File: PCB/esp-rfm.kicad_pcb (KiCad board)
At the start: 2 copper layers, 51.5 x 76.5 mm, 39 parts, among them IC1 RFM69_9X, J3 Conn_Coaxial, J4 USB_C_Receptacle_USB2.0, J5 Conn_01x04, J6 Conn_01x03, Q1 BC847, Q2 BC847, SW1 RST/CONFIG, U1 ESP-12F, U2 AMS1117-3.3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

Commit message: add radio applications cleanup
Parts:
- added U4: USBLC6-2SC6, Package_TO_SOT_SMD:SOT-23-6, F.Cu at (105.1, 122.7)
- moved R13 3.23 mm to (116.9, 122.9)
- moved R12 2.32 mm to (116.9, 119.4)
- moved C6 2.06 mm to (111.1, 115.2)
- moved U3 2.04 mm to (111.2, 121.6)
- moved C7 1.90 mm to (106.3, 118.6)
- moved R6 1.10 mm to (116.9, 117.3)
- moved Q1 1.06 mm to (120.6, 122.0)
- moved R11 0.94 mm to (116.9, 115.2)
- moved Q2 0.59 mm to (120.6, 126.7)
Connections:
- J4 pad A6: Net-(U3-UD+) -> Net-(J4-D+-PadA6)
- J4 pad A7: Net-(U3-UD-) -> Net-(J4-D--PadA7)
- J4 pad B6: Net-(U3-UD+) -> Net-(J4-D+-PadA6)
- J4 pad B7: Net-(U3-UD-) -> Net-(J4-D--PadA7)
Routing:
- net Net-(U3-UD-): track 13.1 -> 2.35 mm, vias 2 -> 0
- net Net-(U3-UD+): track 11.3 -> 2.49 mm, vias 2 -> 0
- net Net-(J4-D--PadA7): track 0.00 -> 8.11 mm
- net Net-(J4-D+-PadA6): track 0.00 -> 6.10 mm, vias 0 -> 2
- net +5V: track 21.4 -> 24.7 mm, vias 2 -> 3
- net Net-(Q2-B): track 2.09 -> 4.89 mm
- net +3.3V: track 210.0 -> 207.8 mm
- net /RST: track 34.6 -> 32.8 mm
- net /RXD: track 25.1 -> 26.6 mm
- net /DQ: track 36.6 -> 35.3 mm
- net /GP0: track 11.8 -> 10.5 mm
- net /TXD: track 24.5 -> 25.8 mm
- net Net-(Q1-B): track 2.09 -> 3.17 mm
- net Net-(Q2-E): track 12.1 -> 12.9 mm
- net GND: track 44.9 -> 44.2 mm, vias 55 -> 56
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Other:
- board text added: "RFM-Gateway www.seegel-systeme.de v1.1 - 27/24"
- board text removed: "RFM-Gateway www.seegel-systeme.de v1.0 - 24/23"

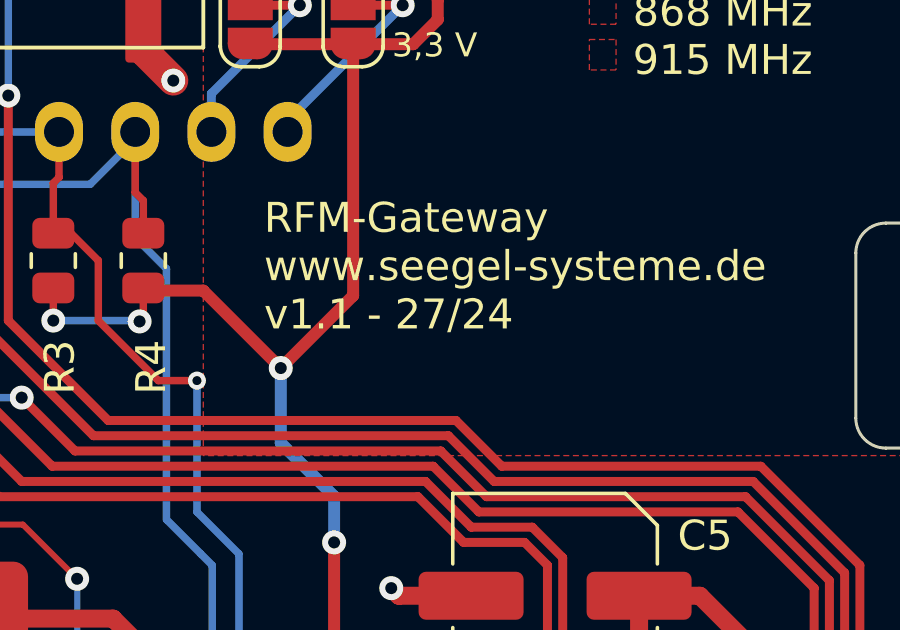
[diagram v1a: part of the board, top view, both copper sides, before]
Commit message: fix warning in platformio.ini
status LED blinker
update PCB
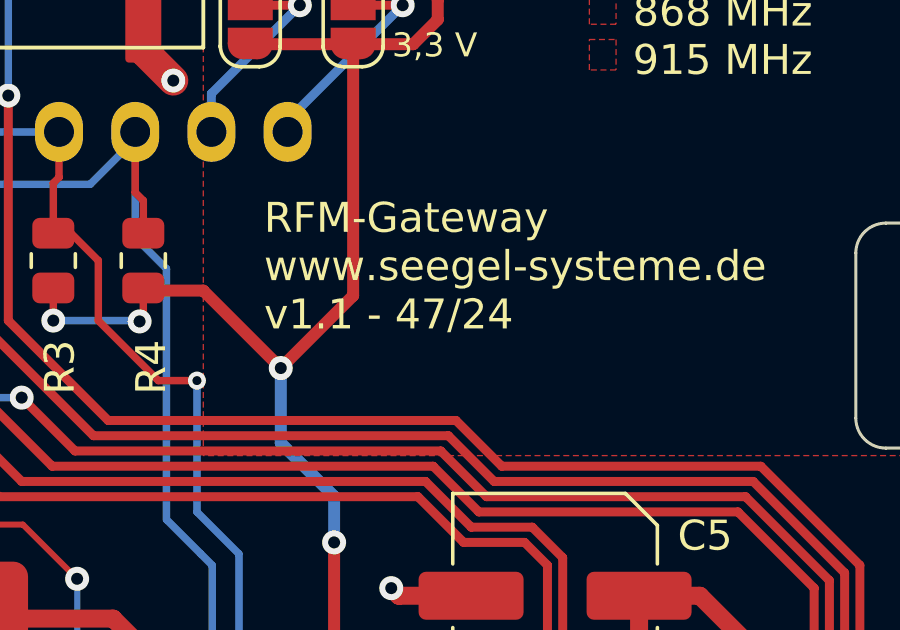
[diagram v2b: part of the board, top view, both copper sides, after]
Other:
- board text added: "RFM-Gateway www.seegel-systeme.de v1.1 - 47/24"
- board text removed: "RFM-Gateway www.seegel-systeme.de v1.1 - 27/24"
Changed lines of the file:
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@@
 		)
 	)
-	(gr_text "RFM-Gateway\nwww.seegel-systeme.de\nv1.1 - 27/24"
+	(gr_text "RFM-Gateway\nwww.seegel-systeme.de\nv1.1 - 47/24"
 		(at 124.0232 100.8836 0)
 		(layer "F.SilkS")

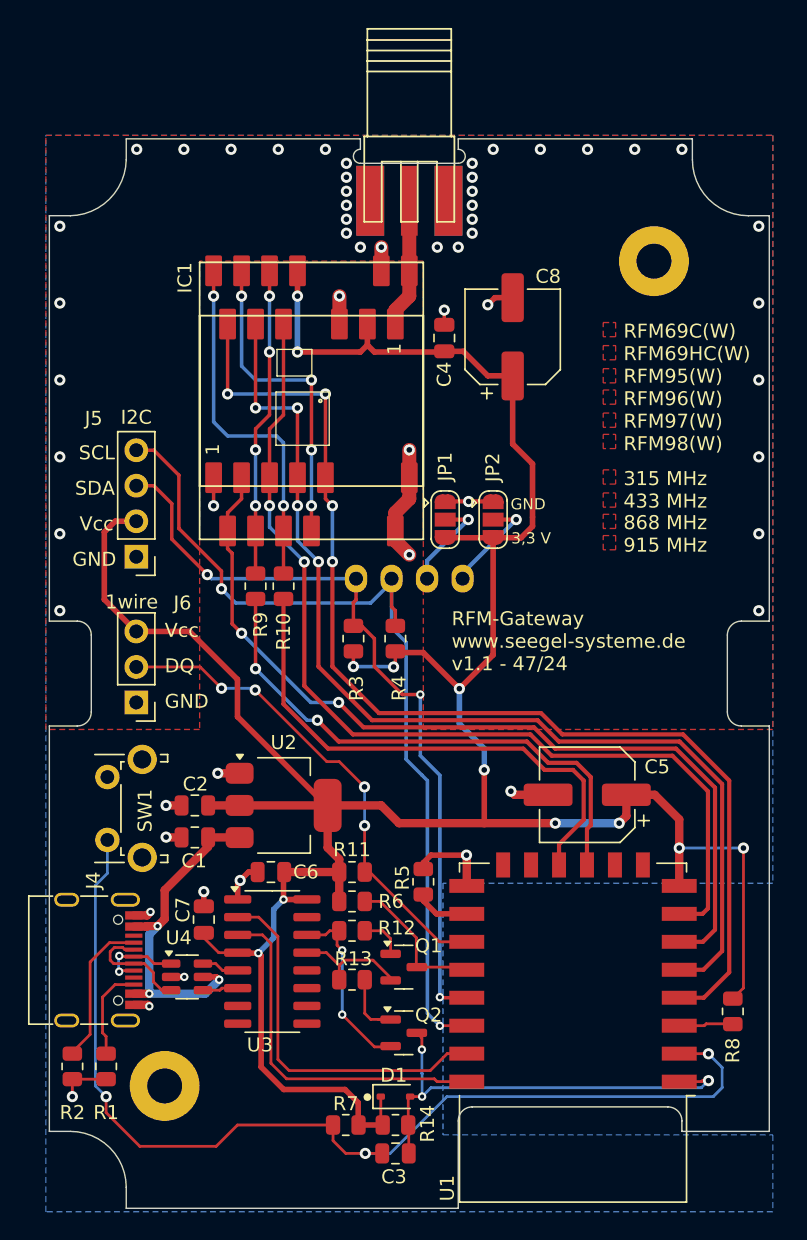
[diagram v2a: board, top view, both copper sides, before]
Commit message: change pin header add ferrite
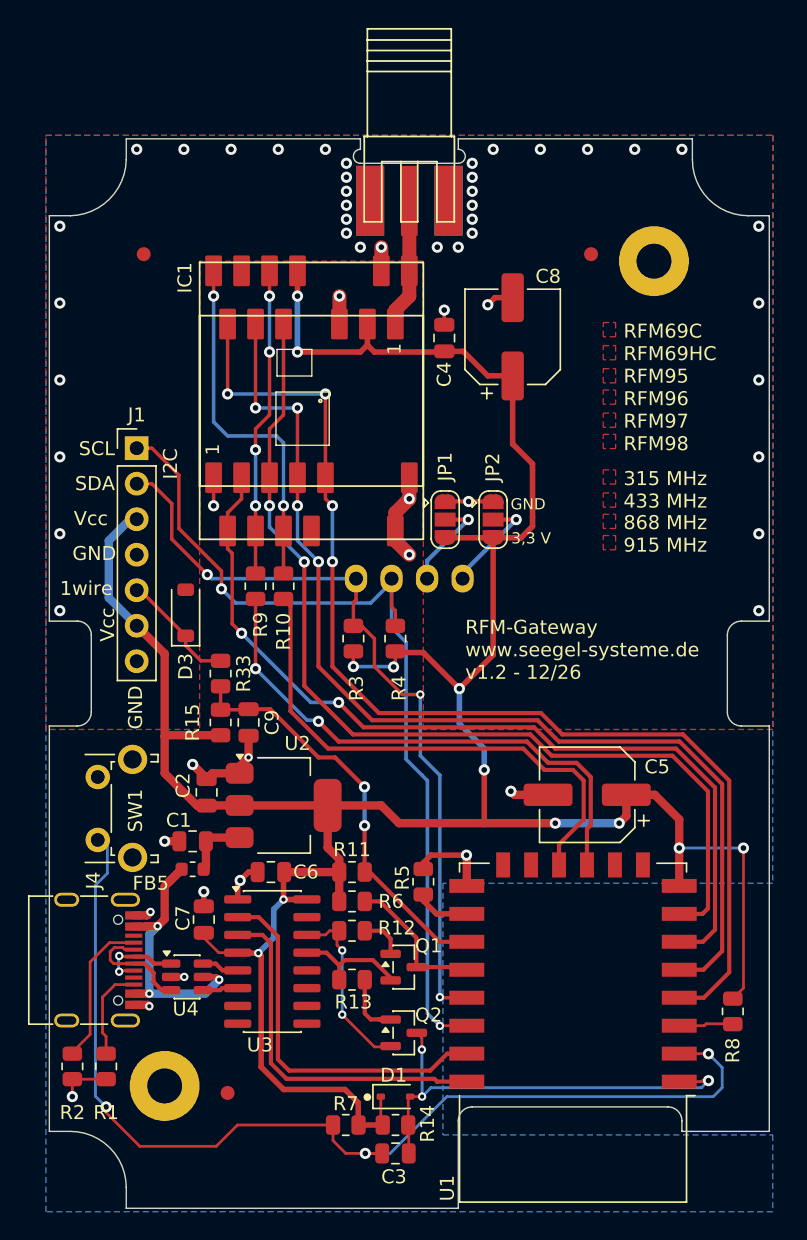
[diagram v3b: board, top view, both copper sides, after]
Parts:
- removed J5: Conn_01x04, Connector_PinHeader_2.54mm:PinHeader_1x04_P2.54mm_Vertical
- removed J6: Conn_01x03, Connector_PinHeader_2.54mm:PinHeader_1x03_P2.54mm_Vertical
- added C9: 470pF, Capacitor_SMD:C_0805_2012Metric, F.Cu at (109.5, 104.5)
- added D3: PTVS3V3S1UR,115, Diode_SMD:D_SOD-123, F.Cu at (105.0, 96.7)
- added FB5: ~, Inductor_SMD:L_0603_1608Metric, F.Cu at (105.5, 115.0)
- added FID1: ~, Fiducial:Fiducial_1mm_Mask2mm, F.Cu at (134.0, 71.0)
- added FID2: ~, Fiducial:Fiducial_1mm_Mask2mm, F.Cu at (108.0, 131.0)
- added FID3: ~, Fiducial:Fiducial_1mm_Mask2mm, F.Cu at (102.0, 71.0)
- added J1: ~, Connector_PinHeader_2.54mm:PinHeader_1x07_P2.54mm_Vertical, F.Cu at (101.5, 84.9)
- added R15: 3k3, Resistor_SMD:R_0805_2012Metric, F.Cu at (107.5, 104.5)
- added R33: 330, Resistor_SMD:R_0805_2012Metric, F.Cu at (107.5, 101.0)
- C1, C2: value 4µ7 -> 10µ
- moved C2 1.26 mm to (106.5, 109.5), turned to 90 degrees
- moved SW1 0.69 mm to (98.7, 112.9)
- moved C1 0.32 mm to (105.5, 113.0)
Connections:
- J4 pad A4: +5V -> +VBUS
- J4 pad A9: +5V -> +VBUS
- J4 pad B4: +5V -> +VBUS
- J4 pad B9: +5V -> +VBUS
- U4 pad 5: +5V -> +VBUS
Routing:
- net unconnected-(IC1-PadDIO1): track 23.0 -> 0.00 mm, vias 4 -> 0
- net +VBUS: track 0.00 -> 20.8 mm, vias 0 -> 3
- net +5V: track 24.7 -> 4.61 mm, vias 3 -> 0
- net Net-(D3-K): track 0.00 -> 8.50 mm
- net /DQ: track 35.3 -> 29.8 mm, vias 4 -> 2
- net GND: track 44.2 -> 46.4 mm
- net +3.3V: track 207.8 -> 206.9 mm
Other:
- board text added: "LCD"
- board text added: "RFM-Gateway www.seegel-systeme.de v1.2 - 12/26"
- board text added: "RFM69C RFM69HC RFM95 RFM96 RFM97 RFM98"
- board text removed: "DQ"
- board text removed: "RFM-Gateway www.seegel-systeme.de v1.1 - 47/24"
- board text removed: "RFM69C(W) RFM69HC(W) RFM95(W) RFM96(W) RFM97(W) RFM98(W)"
